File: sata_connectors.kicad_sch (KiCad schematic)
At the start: 28 parts, among them CN1 HDGCYLSY-SATA-113, CN2 HYCW04-SATA07-129B, Q1 2N7002, Q2 2N7002, U4 TPS259540DSGR, U5 TPS259540DSGR

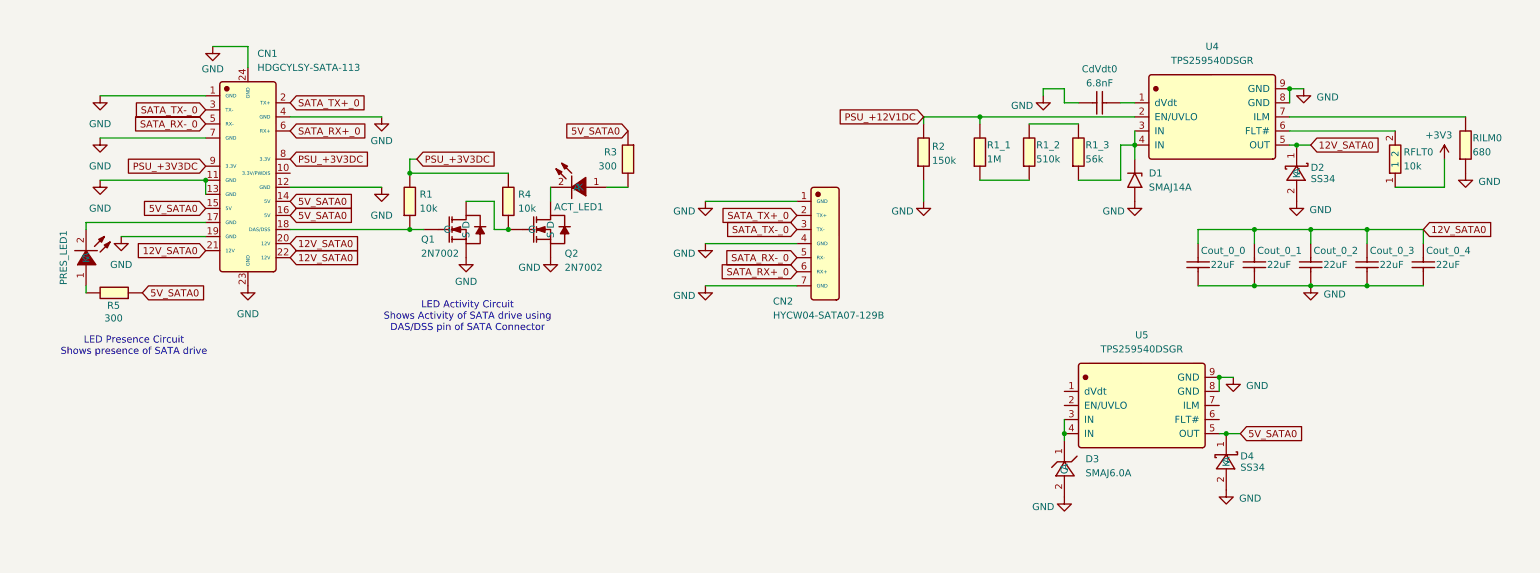
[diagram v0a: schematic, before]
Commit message: updated SATA protections and added MCU control
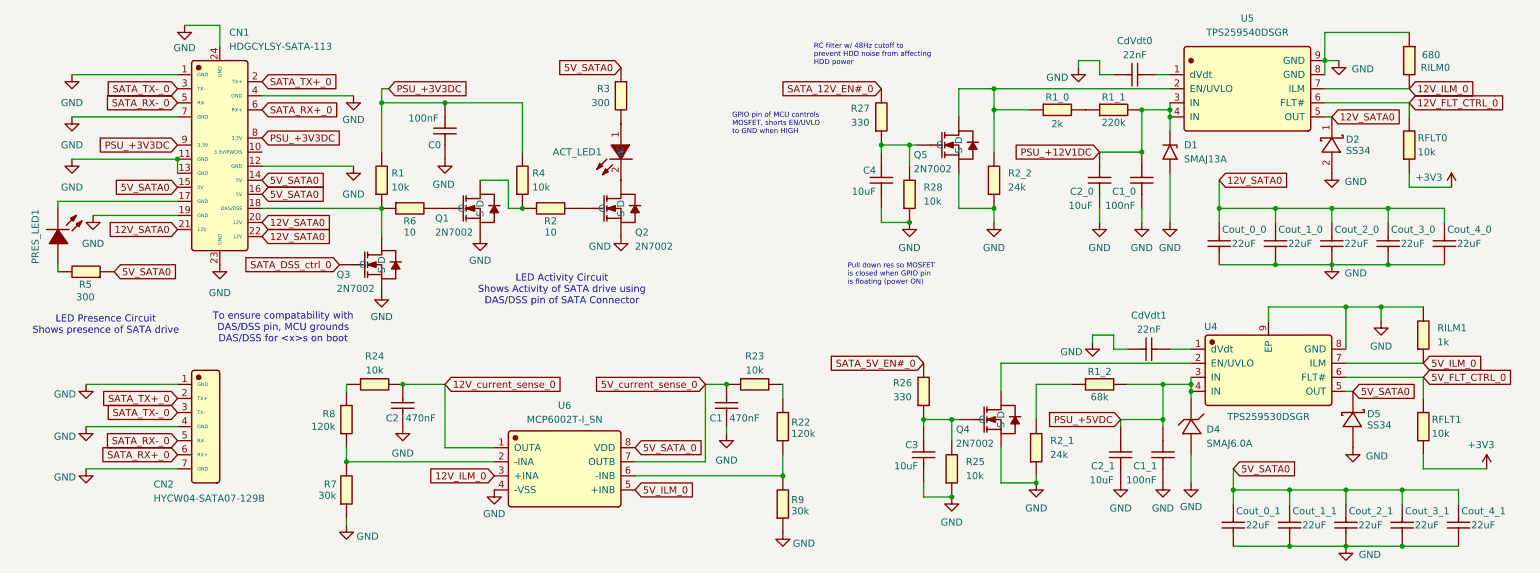
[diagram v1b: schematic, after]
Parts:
- removed CdVdt0: 6.8nF, Capacitor_SMD:C_0603_1608Metric, symbol JLCImport:0603B682K500NT
- removed D1: SMAJ14A, Diode_SMD:D_SMA, symbol Diode:SMAJ14A
- removed R1_1: 1M, Resistor_SMD:R_0603_1608Metric, symbol JLCImport:0603WAF1004T5E
- removed R1_2: 510k, Resistor_SMD:R_0603_1608Metric, symbol JLCImport:0603WAF5103T5E
- removed R1_3: 56k, Resistor_SMD:R_0603_1608Metric, symbol JLCImport:0603WAF5602T5E
- removed R2: 150k, Resistor_SMD:R_0603_1608Metric, symbol JLCImport:0603WAF1503T5E
- removed U4: TPS259540DSGR, Package_SON:WSON-8-1EP_3x3mm_P0.5mm_EP1.2x2mm, symbol JLCImport:TPS259540DSGR
- added C0, C1_0, C1_1: 100nF, Capacitor_SMD:C_0402_1005Metric, symbol JLCImport:CL05B104KB54PNC
- added C1, C2: 470nF, Capacitor_SMD:C_0603_1608Metric, symbol JLCImport:CL10B474KA8NNNC
- added C2_0, C2_1, C3, C4: 10uF, Capacitor_SMD:C_0603_1608Metric, symbol JLCImport:CL10A106KP8NNNC
- added CdVdt0, CdVdt1: 22nF, Capacitor_SMD:C_0603_1608Metric, symbol JLCImport:CL10B223KB8NNNC
- added Cout_0_1, Cout_1_1, Cout_2_1, Cout_3_1, Cout_4_1: 22uF, Capacitor_SMD:C_1206_3216Metric, symbol JLCImport:CL31A226KAHNNNE
- added D1: SMAJ13A, Diode_SMD:D_SMA, symbol Diode:SMAJ13A
- added Q3, Q4, Q5: 2N7002, Package_TO_SOT_SMD:SOT-23-3, symbol JLCImport:2N7002
- added R1_0: 2k, Resistor_SMD:R_0603_1608Metric, symbol JLCImport:0603WAF2001T5E
- added R1_1: 220k, Resistor_SMD:R_0603_1608Metric, symbol JLCImport:0603WAF220KT5E
- added R1_2: 68k, Resistor_SMD:R_0603_1608Metric, symbol JLCImport:0603WAF6802T5E
- added R2, R6: 10, Resistor_SMD:R_0402_1005Metric, symbol JLCImport:0402WGF100JTCE
- added R22, R8: 120k, Resistor_SMD:R_0603_1608Metric, symbol JLCImport:0603WAF1203T5E
- added R23, R24, R25, R28, RFLT1: 10k, Resistor_SMD:R_0402_1005Metric, symbol JLCImport:0402WGF1002TCE
- added R26, R27: 330, Resistor_SMD:R_0402_1005Metric, symbol JLCImport:0402WGF3300TCE
- added R2_1, R2_2: 24k, Resistor_SMD:R_0603_1608Metric, symbol JLCImport:0603WAF2402T5E
- added R7, R9: 30k, Resistor_SMD:R_0603_1608Metric, symbol JLCImport:0603WAF3002T5E
- added RILM1: 1k, Resistor_SMD:R_0603_1608Metric, symbol JLCImport:0603WAF1001T5E
- added U4: TPS259530DSGR, Package_SON:WSON-8-1EP_3x3mm_P0.5mm_EP1.2x2mm, symbol JLCImport:TPS259530DSGR
- added U6: MCP6002T-I_SN, JLCImport:MCP6002T-I_SN, symbol JLCImport:MCP6002T-I_SN
- renumbered Cout_0_1 to Cout_1_0, Cout_0_2 to Cout_2_0, Cout_0_3 to Cout_3_0, Cout_0_4 to Cout_4_0, D3 to D4, D4 to D5
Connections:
- net +3V3: now also RFLT1.1
- net 12V_SATA0: now also U5.5 (OUT)
- net 5V_SATA0: now also Cout_0_1.2, Cout_1_1.2, Cout_2_1.2, Cout_3_1.2, Cout_4_1.2, U4.5 (OUT); no longer U5.5 (OUT)
- net GND: now also C0.1, C1.1, C1_0.1, C1_1.1, C2.1, C2_0.1, C2_1.1, C3.1, C4.1, CdVdt0.1, CdVdt1.1, Cout_0_1.1, Cout_1_1.1, Cout_2_1.1, Cout_3_1.1, Cout_4_1.1, D1.2 (A2), Q3.2 (S), Q4.2 (S), Q5.2 (S), R25.1, R28.1, R2_1.1, R2_2.1, R7.1, R9.1, RILM1.2, U4.8 (GND), U4.9 (EP), U6.4 (-VSS)
- net PSU_+12V1DC: now also U5.3 (IN), U5.4 (IN), C1_0.2, C2_0.2, D1.1 (A1), R1_1.2
- net PSU_+3V3DC: now also C0.2
- net at Q1.3 (D), R4.1: now also R2.1; no longer Q2.1 (G)
- net 12V_FLT_CTRL_0: now reaches RFLT0.2
- net 12V_FLT_CTRL_0: now also U5.6 (FLT#)
- net 12V_ILM_0: now reaches RILM0.2
- net 12V_ILM_0: now also U5.7 (ILM), U6.3 (+INA)
- net at CN1.18 (DAS/DSS), R1.1: now also Q3.3 (D), R6.1; no longer Q1.1 (G)
- net at U5.1 (dVdt): now also CdVdt0.2
- net at U5.2 (EN/UVLO): now also Q5.3 (D), R1_0.1, R2_2.2
- new net: Q1.1 (G), R6.2
- new net: R22.2, R23.2
- new net: R1_0.2, R1_1.1
- new net: CdVdt1.2, U4.1 (dVdt)
- new net: C3.2, Q4.1 (G), R25.2, R26.1
- new net: Q4.3 (D), U4.2 (EN/UVLO)
- new net: C4.2, Q5.1 (G), R27.1, R28.2
- new net: R24.1, R8.2
- new net: R7.2, R8.1, U6.2 (-INA)
- new net: Q2.1 (G), R2.2
- new net: R1_2.1, R2_1.2
- new net: R22.1, R9.2, U6.6 (-INB)
- new net 12V_current_sense_0: C2.2, R24.2, U6.1 (OUTA)
- new net 5V_FLT_CTRL_0: RFLT1.2, U4.6 (FLT#)
- new net 5V_ILM_0: RILM1.1, U4.7 (ILM), U6.5 (+INB)
- new net 5V_SATA_0: U6.8 (VDD)
- new net 5V_current_sense_0: C1.2, R23.1, U6.7 (OUTB)
- new net PSU_+5VDC: C1_1.2, C2_1.2, D4.1 (C), R1_2.2, U4.3 (IN), U4.4 (IN)
- new net SATA_12V_EN#_0: R27.2
- new net SATA_5V_EN#_0: R26.2
- new net SATA_DSS_ctrl_0: Q3.1 (G)
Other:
- note added: "GPIO pin of MCU controls MOSFET, shorts EN/UVLO to GND when HIGH"
- note added: "Pull down res so MOSFET is closed when GPIO pin is floating (power ON)"
- note added: "RC filter w/ 48Hz cutoff to prevent HDD noise from affecting HDD power"
- note added: "To ensure compatability with DAS/DSS pin, MCU grounds DAS/DSS for <x>s on boot"
- moved on the sheet: ACT_LED1, CN1, CN2, Cout_0_0, Cout_1_0, Cout_2_0, Cout_3_0, Cout_4_0, Q1, Q2, R1, R3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
